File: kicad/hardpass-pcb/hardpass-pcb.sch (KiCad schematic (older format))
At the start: 55 parts, among them P1 Pi_Zero, P2 OLED_I2C, SW1 1, SW10 C/UP, SW11 0/OK, SW12 OK/DN, SW13 SHUTDN, SW14 SW_PUSH_SMALL, SW2 2, SW3 3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

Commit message: routed 2nd board
not finished, but a start
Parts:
- P3: renamed from P?; footprint Pin_Headers:Pin_Header_Straight_2x20_Pitch2.54mm -> hardpass:Pin_Header_Straight_2x20_Pitch2.54mm_centered
- Y1: footprint (none) -> Crystals:Crystal_HC49-U_Vertical
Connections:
- net +5V: now also U1.9 (K1), U3.8 (PRES)
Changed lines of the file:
@@
 ROW_4
 $Comp
-L GND #PWR1
+L GND #PWR01
 U 1 1 57211ADA
 P 1000 3100
-F 0 "#PWR1" H 1000 2850 50  0001 C CNN
+F 0 "#PWR01" H 1000 2850 50  0001 C CNN
 F 1 "GND" H 1000 2950 50  0000 C CNN
 F 2 "" H 1000 3100 50  0000 C CNN
@@
 $EndComp
 $Comp
-L +3.3V #PWR2
+L +3.3V #PWR02
 U 1 1 57211B7B
 P 1050 950
-F 0 "#PWR2" H 1050 800 50  0001 C CNN
+F 0 "#PWR02" H 1050 800 50  0001 C CNN
 F 1 "+3.3V" H 1050 1090 50  0000 C CNN
 F 2 "" H 1050 950 50  0000 C CNN
@@
 SD_D1
 $Comp
-L GND #PWR3
+L GND #PWR03
 U 1 1 5723909B
 P 3000 3100
-F 0 "#PWR3" H 3000 2850 50  0001 C CNN
+F 0 "#PWR03" H 3000 2850 50  0001 C CNN
 F 1 "GND" H 3000 2950 50  0000 C CNN
 F 2 "" H 3000 3100 50  0000 C CNN
@@
 $EndComp
 $Comp
-L GND #PWR15
+L GND #PWR04
 U 1 1 576AFDF4
 P 5150 900
-F 0 "#PWR15" H 5150 650 50  0001 C CNN
+F 0 "#PWR04" H 5150 650 50  0001 C CNN
 F 1 "GND" H 5150 750 50  0001 C CNN
 F 2 "" H 5150 900 50  0000 C CNN
@@
 OLED_SCL
 $Comp
-L +3.3V #PWR12
+L +3.3V #PWR05
 U 1 1 576B9B60
 P 4850 2650
-F 0 "#PWR12" H 4850 2500 50  0001 C CNN
+F 0 "#PWR05" H 4850 2500 50  0001 C CNN
 F 1 "+3.3V" H 4850 2790 50  0001 C CNN
 F 2 "" H 4850 2650 50  0000 C CNN
@@
 $EndComp
 $Comp
-L GND #PWR13
+L GND #PWR06
 U 1 1 576B9D6C
 P 4950 3950
-F 0 "#PWR13" H 4950 3700 50  0001 C CNN
+F 0 "#PWR06" H 4950 3700 50  0001 C CNN
 F 1 "GND" H 4950 3800 50  0001 C CNN
 F 2 "" H 4950 3950 50  0000 C CNN
@@
 SHUTDOWN
 $Comp
-L GND #PWR4
+L GND #PWR07
 U 1 1 57716417
 P 3800 7050
-F 0 "#PWR4" H 3800 6800 50  0001 C CNN
+F 0 "#PWR07" H 3800 6800 50  0001 C CNN
 F 1 "GND" H 3800 6900 50  0000 C CNN
 F 2 "" H 3800 7050 50  0000 C CNN
@@
 Wifi Pants: \n    pin 27-->
 $Comp
-L GND #PWR6
+L GND #PWR08
 U 1 1 58333C64
 P 4500 1850
-F 0 "#PWR6" H 4500 1600 50  0001 C CNN
+F 0 "#PWR08" H 4500 1600 50  0001 C CNN
 F 1 "GND" H 4500 1700 50  0001 C CNN
 F 2 "" H 4500 1850 50  0000 C CNN
@@
 $EndComp
 $Comp
-L +3.3V #PWR11
+L +3.3V #PWR09
 U 1 1 58333EC0
 P 4700 1850
-F 0 "#PWR11" H 4700 1700 50  0001 C CNN
+F 0 "#PWR09" H 4700 1700 50  0001 C CNN
 F 1 "+3.3V" H 4700 1990 50  0001 C CNN
 F 2 "" H 4700 1850 50  0000 C CNN
@@
 $EndComp
 $Comp
-L +3.3V #PWR7
+L +3.3V #PWR010
 U 1 1 58337E9C
 P 4550 2150
-F 0 "#PWR7" H 4550 2000 50  0001 C CNN
+F 0 "#PWR010" H 4550 2000 50  0001 C CNN
 F 1 "+3.3V" H 4550 2290 50  0001 C CNN
 F 2 "" H 4550 2150 50  0000 C CNN
@@
 $EndComp
 $Comp
-L GND #PWR8
+L GND #PWR011
 U 1 1 58337F0D
 P 4550 2550
-F 0 "#PWR8" H 4550 2300 50  0001 C CNN
+F 0 "#PWR011" H 4550 2300 50  0001 C CNN
 F 1 "GND" H 4550 2400 50  0001 C CNN
 F 2 "" H 4550 2550 50  0000 C CNN
@@
 NoConn ~ 6600 5500
 $Comp
-L GND #PWR19
+L GND #PWR012
 U 1 1 57B89D14
 P 6600 5700
-F 0 "#PWR19" H 6600 5450 50  0001 C CNN
+F 0 "#PWR012" H 6600 5450 50  0001 C CNN
 F 1 "GND" H 6600 5550 50  0000 C CNN
 F 2 "" H 6600 5700 50  0000 C CNN
@@
 NoConn ~ 4800 5100
 $Comp
-L +3V3 #PWR9
+L +3V3 #PWR013
 U 1 1 57B89D90
 P 4600 5700
-F 0 "#PWR9" H 4600 5550 50  0001 C CNN
+F 0 "#PWR013" H 4600 5550 50  0001 C CNN
 F 1 "+3V3" H 4600 5840 50  0000 C CNN
 F 2 "" H 4600 5700 50  0000 C CNN
@@
 $EndComp
 $Comp
-L GND #PWR5
+L GND #PWR014
 U 1 1 5870295E
 P 4500 1550
-F 0 "#PWR5" H 4500 1300 50  0001 C CNN
+F 0 "#PWR014" H 4500 1300 50  0001 C CNN
 F 1 "GND" H 4500 1400 50  0001 C CNN
 F 2 "" H 4500 1550 50  0000 C CNN
@@
 $EndComp
 $Comp
-L +3.3V #PWR10
+L +3.3V #PWR015
 U 1 1 58702964
 P 4700 1550
-F 0 "#PWR10" H 4700 1400 50  0001 C CNN
+F 0 "#PWR015" H 4700 1400 50  0001 C CNN
 F 1 "+3.3V" H 4700 1690 50  0001 C CNN
 F 2 "" H 4700 1550 50  0000 C CNN
@@
 NoConn ~ 5250 1650
 $Comp
-L GND #PWR14
+L GND #PWR016
 U 1 1 58702A61
 P 5000 2000
-F 0 "#PWR14" H 5000 1750 50  0001 C CNN
+F 0 "#PWR016" H 5000 1750 50  0001 C CNN
 F 1 "GND" H 5000 1850 50  0001 C CNN
 F 2 "" H 5000 2000 50  0000 C CNN
@@
 $EndComp
 $Comp
-L +3.3V #PWR17
+L +3.3V #PWR017
 U 1 1 58702DF8
 P 5150 2100
-F 0 "#PWR17" H 5150 1950 50  0001 C CNN
+F 0 "#PWR017" H 5150 1950 50  0001 C CNN
 F 1 "+3.3V" H 5150 2240 50  0001 C CNN
 F 2 "" H 5150 2100 50  0000 C CNN
@@
 $EndComp
 $Comp
-L GND #PWR16
+L GND #PWR018
 U 1 1 58702F8A
 P 5150 1700
-F 0 "#PWR16" H 5150 1450 50  0001 C CNN
+F 0 "#PWR018" H 5150 1450 50  0001 C CNN
 F 1 "GND" H 5150 1550 50  0001 C CNN
 F 2 "" H 5150 1700 50  0000 C CNN
@@
 $EndComp
 $Comp
-L GND #PWR18
+L GND #PWR019
 U 1 1 58705FA1
 P 5150 2450
-F 0 "#PWR18" H 5150 2200 50  0001 C CNN
+F 0 "#PWR019" H 5150 2200 50  0001 C CNN
 F 1 "GND" H 5150 2300 50  0001 C CNN
 F 2 "" H 5150 2450 50  0000 C CNN
@@
 NoConn ~ 9600 1700
 $Comp
-L GND #PWR29
+L GND #PWR020
 U 1 1 5880D50E
 P 10150 1700
-F 0 "#PWR29" H 10150 1450 50  0001 C CNN
+F 0 "#PWR020" H 10150 1450 50  0001 C CNN
 F 1 "GND" H 10150 1550 50  0000 C CNN
 F 2 "" H 10150 1700 50  0000 C CNN
@@
 $EndComp
 $Comp
-L GND #PWR33
+L GND #PWR021
 U 1 1 5881377E
 P 10900 2600
-F 0 "#PWR33" H 10900 2350 50  0001 C CNN
+F 0 "#PWR021" H 10900 2350 50  0001 C CNN
 F 1 "GND" H 10900 2450 50  0000 C CNN
 F 2 "" H 10900 2600 50  0000 C CNN
@@
 $EndComp
 $Comp
-L GND #PWR26
+L GND #PWR022
 U 1 1 5881836B
 P 9700 3700
-F 0 "#PWR26" H 9700 3450 50  0001 C CNN
+F 0 "#PWR022" H 9700 3450 50  0001 C CNN
 F 1 "GND" H 9700 3550 50  0000 C CNN
 F 2 "" H 9700 3700 50  0000 C CNN
@@
 $EndComp
 $Comp
-L GND #PWR21
+L GND #PWR023
 U 1 1 5881F197
 P 8450 2550
-F 0 "#PWR21" H 8450 2300 50  0001 C CNN
+F 0 "#PWR023" H 8450 2300 50  0001 C CNN
 F 1 "GND" H 8450 2400 50  0001 C CNN
 F 2 "" H 8450 2550 50  0000 C CNN
@@
 $EndComp
 $Comp
-L GND #PWR28
+L GND #PWR024
 U 1 1 58833208
 P 10000 4200
-F 0 "#PWR28" H 10000 3950 50  0001 C CNN
+F 0 "#PWR024" H 10000 3950 50  0001 C CNN
 F 1 "GND" H 10000 4050 50  0000 C CNN
 F 2 "" H 10000 4200 50  0000 C CNN
@@
 TODO: less Caps?
 $Comp
-L GND #PWR24
+L GND #PWR025
 U 1 1 58839D11
 P 9300 3400
-F 0 "#PWR24" H 9300 3150 50  0001 C CNN
+F 0 "#PWR025" H 9300 3150 50  0001 C CNN
 F 1 "GND" H 9300 3250 50  0000 C CNN
 F 2 "" H 9300 3400 50  0000 C CNN
@@
 F 0 "Y1" H 9850 1450 50  0000 C CNN
 F 1 "14.745MHz" H 9850 1150 50  0000 C CNN
-F 2 "" H 9850 1300 50  0000 C CNN
+F 2 "Crystals:Crystal_HC49-U_Vertical" H 9850 1300 50  0001 C CNN
 F 3 "" H 9850 1300 50  0000 C CNN
 	1    9850 1300
@@
 $EndComp
 $Comp
-L GND #PWR27
+L GND #PWR026
 U 1 1 5883AC0F
 P 9850 900
-F 0 "#PWR27" H 9850 650 50  0001 C CNN
+F 0 "#PWR026" H 9850 650 50  0001 C CNN
 F 1 "GND" H 9850 750 50  0000 C CNN
 F 2 "" H 9850 900 50  0000 C CNN
@@
 $EndComp
 $Comp
-L GND #PWR32
+L GND #PWR027
 U 1 1 5883C802
 P 10650 2800
-F 0 "#PWR32" H 10650 2550 50  0001 C CNN
+F 0 "#PWR027" H 10650 2550 50  0001 C CNN
 F 1 "GND" H 10650 2650 50  0000 C CNN
 F 2 "" H 10650 2800 50  0000 C CNN
@@
 possible driver: https://github.com/larytet/TDA8029
 $Comp
-L +5V #PWR22
+L +5V #PWR028
 U 1 1 588108E7
 P 8600 1950
-F 0 "#PWR22" H 8600 1800 50  0001 C CNN
+F 0 "#PWR028" H 8600 1800 50  0001 C CNN
 F 1 "+5V" H 8600 2090 50  0000 C CNN
 F 2 "" H 8600 1950 50  0000 C CNN
@@
 $EndComp
 $Comp
-L +5V #PWR23
+L +5V #PWR029
 U 1 1 58810991
 P 8800 2200
-F 0 "#PWR23" H 8800 2050 50  0001 C CNN
+F 0 "#PWR029" H 8800 2050 50  0001 C CNN
 F 1 "+5V" H 8800 2340 50  0000 C CNN
 F 2 "" H 8800 2200 50  0000 C CNN
@@
 $EndComp
 $Comp
-L +5V #PWR31
+L +5V #PWR030
 U 1 1 58810A71
 P 10650 2500
-F 0 "#PWR31" H 10650 2350 50  0001 C CNN
+F 0 "#PWR030" H 10650 2350 50  0001 C CNN
 F 1 "+5V" H 10650 2640 50  0000 C CNN
 F 2 "" H 10650 2500 50  0000 C CNN
@@
 $EndComp
 $Comp
-L +5V #PWR30
+L +5V #PWR031
 U 1 1 58810B51
 P 10200 3400
-F 0 "#PWR30" H 10200 3250 50  0001 C CNN
+F 0 "#PWR031" H 10200 3250 50  0001 C CNN
 F 1 "+5V" H 10200 3540 50  0000 C CNN
 F 2 "" H 10200 3400 50  0000 C CNN
@@
 $EndComp
 $Comp
-L +5V #PWR25
+L +5V #PWR032
 U 1 1 588110F4
 P 9500 1500
-F 0 "#PWR25" H 9500 1350 50  0001 C CNN
+F 0 "#PWR032" H 9500 1350 50  0001 C CNN
 F 1 "+5V" H 9500 1640 50  0000 C CNN
 F 2 "" H 9500 1500 50  0000 C CNN
@@
 $EndComp
 $Comp
-L +5V #PWR20
+L +5V #PWR033
 U 1 1 588119E7
 P 7550 2900
-F 0 "#PWR20" H 7550 2750 50  0001 C CNN
+F 0 "#PWR033" H 7550 2750 50  0001 C CNN
 F 1 "+5V" H 7550 3040 50  0000 C CNN
 F 2 "" H 7550 2900 50  0000 C CNN
@@
 http://www.linkconn.com/en/product/\ne08f128a-897a-4361-86f3-81b7a41ba7d4\n'sim card samsung i9000 n7000'
 $Comp
-L CONN_02X20 P?
+L CONN_02X20 P3
 U 1 1 5881588C
 P 8800 5250
-F 0 "P?" H 8800 6300 50  0000 C CNN
+F 0 "P3" H 8800 6300 50  0000 C CNN
 F 1 "Pi_Zero" V 8800 5250 50  0000 C CNN
-F 2 "Pin_Headers:Pin_Header_Straight_2x20_Pitch2.54mm" H 8800 3900 50  0001 C CNN
+F 2 "hardpass:Pin_Header_Straight_2x20_Pitch2.54mm_centered" H 8800 3900 50  0001 C CNN
 F 3 "" H 8800 4300 50  0000 C CNN
 	1    8800 5250
@@
 $EndComp
 $Comp
-L +5V #PWR?
+L +5V #PWR034
 U 1 1 58817164
 P 9150 4300
-F 0 "#PWR?" H 9150 4150 50  0001 C CNN
+F 0 "#PWR034" H 9150 4150 50  0001 C CNN
 F 1 "+5V" H 9150 4440 50  0000 C CNN
 F 2 "" H 9150 4300 50  0000 C CNN
@@
 $EndComp
 $Comp
-L GND #PWR?
+L GND #PWR035
 U 1 1 5881733E
 P 8450 6200
-F 0 "#PWR?" H 8450 5950 50  0001 C CNN
+F 0 "#PWR035" H 8450 5950 50  0001 C CNN
 F 1 "GND" H 8450 6050 50  0000 C CNN
 F 2 "" H 8450 6200 50  0000 C CNN
@@
 $EndComp
 $Comp
-L GND #PWR?
+L GND #PWR036
 U 1 1 588173EB
 P 9150 6200
-F 0 "#PWR?" H 9150 5950 50  0001 C CNN
+F 0 "#PWR036" H 9150 5950 50  0001 C CNN
 F 1 "GND" H 9150 6050 50  0000 C CNN
 F 2 "" H 9150 6200 50  0000 C CNN
@@
 	7750 3400 9300 3400
 Wire Wire Line
-	7700 3000 7450 3000
-Wire Wire Line
-	7700 2900 7700 3000
-Wire Wire Line
-	8800 2900 7700 2900
+	7150 3000 7700 3000
+Wire Wire Line
+	7700 3000 7700 2900
+Wire Wire Line
+	7700 2900 8800 2900
 Wire Wire Line
 	7700 2800 7700 2650
@@
 Connection ~ 8600 2600
 Wire Wire Line
-	7450 2900 7550 2900
+	7150 2900 7550 2900
 Wire Wire Line
 	7450 3200 7600 3200
@@
 Wire Notes Line
 	6150 650  6150 4250
+Wire Wire Line
+	7150 3000 7150 2900
+Connection ~ 7450 2900
+Connection ~ 7450 3000
 $EndSCHEMATC

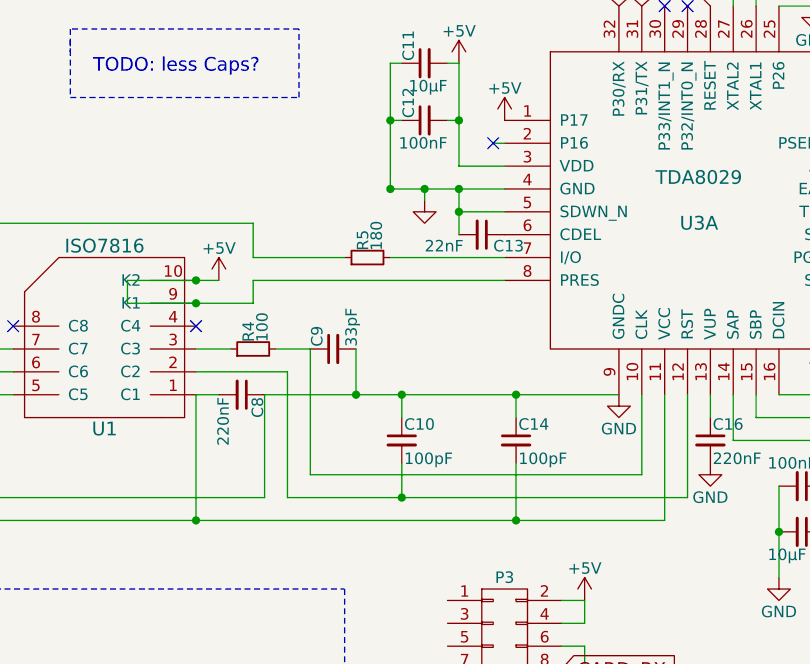
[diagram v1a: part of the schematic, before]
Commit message: fixed bug (shdn_N), removed caps
according to data sheet, shdn_n needs to be high to activate card (page43)

2 bypass caps have been removed according to page 8 of AN00046
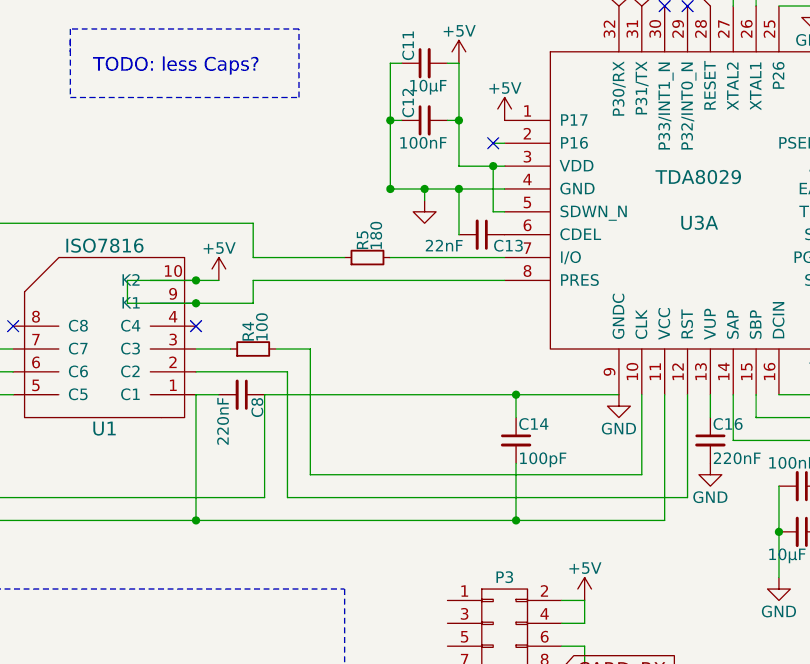
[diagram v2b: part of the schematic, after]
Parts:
- removed C10: 100pF, Capacitors_SMD:C_1206, symbol C_Small
- removed C9: 33pF, Capacitors_SMD:C_1206, symbol C_Small
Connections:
- net +5V: now also U3.5 (SDWN_N)
- net GND: no longer U3.5 (SDWN_N)
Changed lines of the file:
@@
-$EndComp
-$Comp
-L C_Small C10
-U 1 1 5880BC62
-P 8350 3600
-F 0 "C10" H 8360 3670 50  0000 L CNN
-F 1 "100pF" H 8360 3520 50  0000 L CNN
-F 2 "Capacitors_SMD:C_1206" H 8350 3600 50  0001 C CNN
-F 3 "" H 8350 3600 50  0000 C CNN
-	1    8350 3600
-	1    0    0    -1
 $EndComp
 $Comp
@@
 $EndComp
 $Comp
-L C_Small C9
-U 1 1 5882B77E
-P 8050 3200
-F 0 "C9" H 8060 3270 50  0000 L CNN
-F 1 "33pF" H 8060 3120 50  0000 L CNN
-F 2 "Capacitors_SMD:C_1206" H 8050 3200 50  0001 C CNN
-F 3 "" H 8050 3200 50  0000 C CNN
-	1    8050 3200
-	0    -1   -1   0
-$EndComp
-$Comp
 L C_Small C14
 U 1 1 588317FD
@@
 	1    0    0    -1
 $EndComp
-Connection ~ 8150 3400
-Wire Wire Line
-	8150 3200 8150 3400
 Wire Wire Line
 	7750 3850 7750 3400
@@
 	4600 5700 4800 5700
 Wire Wire Line
-	8350 3700 8350 3850
-Connection ~ 8350 3850
-Wire Wire Line
-	8350 3500 8350 3400
-Connection ~ 8350 3400
-Wire Wire Line
 	8850 3500 8850 3400
 Connection ~ 8850 3400
@@
 Connection ~ 8600 2500
 Wire Wire Line
-	8800 2600 8600 2600
-Connection ~ 8600 2600
-Wire Wire Line
 	7150 2900 7550 2900
 Wire Wire Line
@@
 Connection ~ 7450 2900
 Connection ~ 7450 3000
+Wire Wire Line
+	8800 2600 8750 2600
+Wire Wire Line
+	8750 2600 8750 2400
+Connection ~ 8750 2400
 $EndSCHEMATC
